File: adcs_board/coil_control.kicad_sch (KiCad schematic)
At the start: 9 parts, among them U5 DRV8210DSGR, U6 DRV8210DSGR, U7 DRV8210DSGR

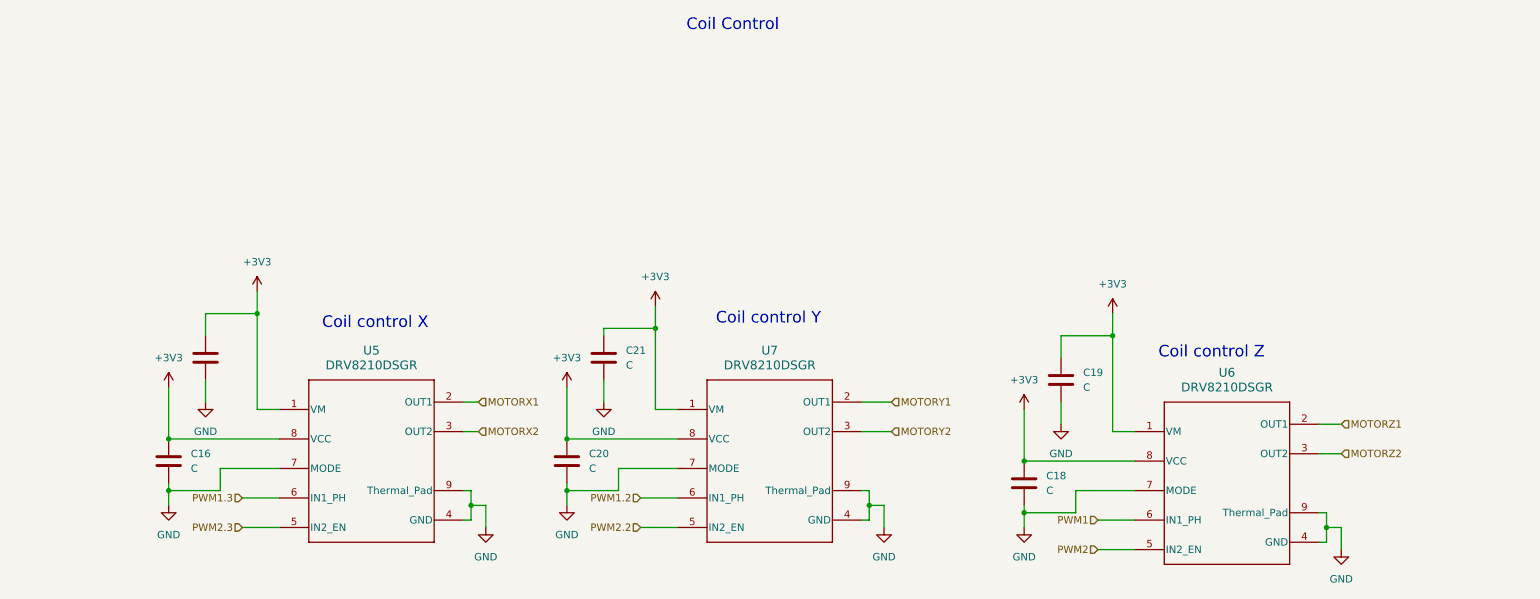
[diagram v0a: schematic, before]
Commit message: adcs_board: resolve schematic ERC violations
- Corrected electrical rule check (ERC) errors in ADCS BDOT schematic
- Fixed unconnected pins and mismatched power nets
- Adjusted symbol properties for proper ERC compliance
- Ensured clean schematic validation with no remaining ERC issues
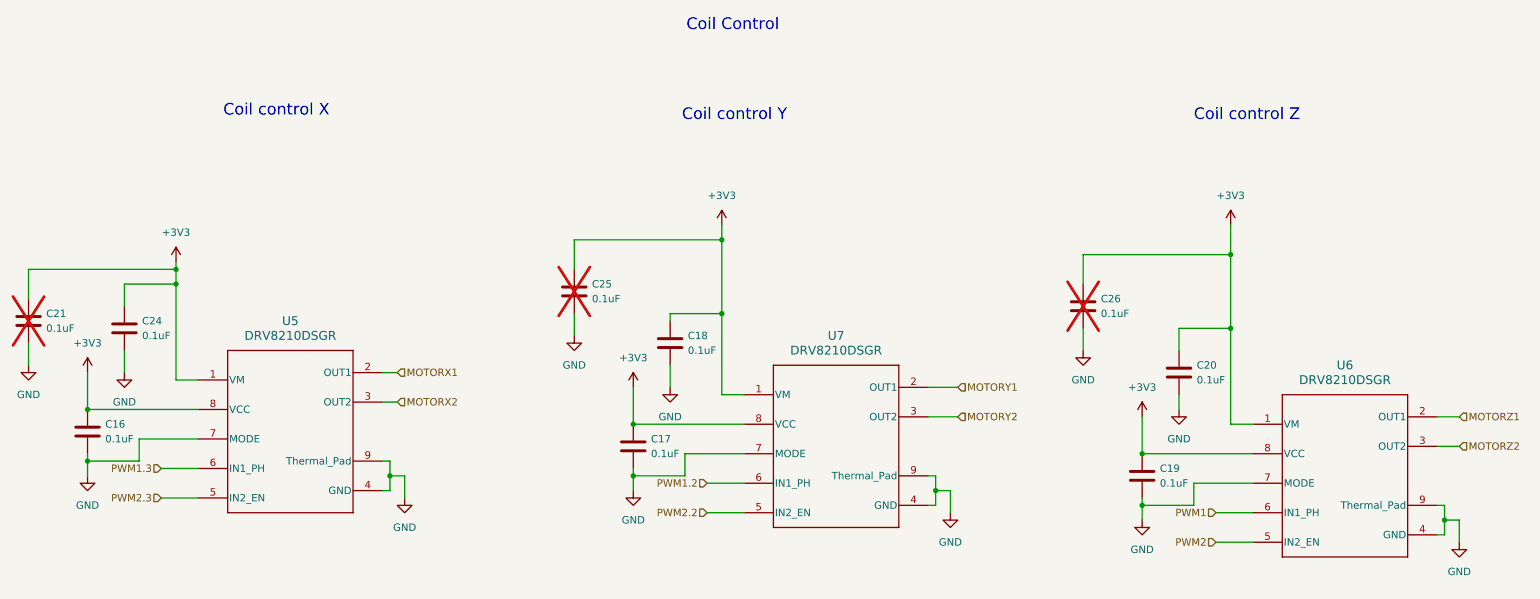
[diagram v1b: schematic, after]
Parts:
- added C24, C25, C26: 0.1uF, Capacitor_SMD:C_0201_0603Metric, symbol Device:C
- C16, C17, C18, C19, C20: value C -> 0.1uF; footprint (none) -> Capacitor_SMD:C_0201_0603Metric; Manufacturer (none) -> YAGEO; Manufacturer Part Number (none) -> CC0603KRX7R7BB104
- C21: value C -> 0.1uF; footprint (none) -> Capacitor_SMD:C_0201_0603Metric; now not fitted; now left out of the parts list
- U5, U6, U7: footprint adcs:DSG0008A-IPC_A -> adcs:DSG0008A-IPC_C
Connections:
- net +3V3: now also C24.1, C25.1, C26.1
- net GND: now also C24.2, C25.2, C26.2
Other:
- title: (none) -> ADCS-BDOT
